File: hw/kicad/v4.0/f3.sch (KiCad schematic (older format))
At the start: 34 parts, among them P11 USB_OTG, P12 CONN_01X04, P7 CONN_01X04, T1 testpoint, T2 testpoint, T44 testpoint, T45 testpoint, T46 testpoint, U21 USBLC6-4SC6, U25 STM32F303CBTx, U29 USBLC6-4SC6, Y1 8M

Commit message: update TVS LCSC part number
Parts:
- U21, U29: LCSC C252436 -> C435848
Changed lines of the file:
@@
 EESchema Schematic File Version 4
-LIBS:stmbl_4.0-cache
 EELAYER 30 0
 EELAYER END
@@
 F 9 "" H 0   0   50  0001 C CNN "InternalName"
 F 10 "STMicroelectronics" H 0   0   50  0001 C CNN "Manufacturer"
-F 11 "C252436" H 9400 6600 50  0001 C CNN "LCSC"
+F 11 "C435848" H 9400 6600 50  0001 C CNN "LCSC"
 	1    9400 6600
 	1    0    0    -1
@@
 F 9 "" H 0   0   50  0001 C CNN "InternalName"
 F 10 "STMicroelectronics" H 0   0   50  0001 C CNN "Manufacturer"
-F 11 "C252436" H 4350 5650 50  0001 C CNN "LCSC"
+F 11 "C435848" H 4350 5650 50  0001 C CNN "LCSC"
 	1    4350 5650
 	1    0    0    -1

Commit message: Changed 120uf 1808 to 1210 100uF
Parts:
- C10, C128, C2, C7, C78, C79, C82, C83, C9: LCSC C14663 -> C14663
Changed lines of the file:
@@
 F 9 "" H 0   0   50  0001 C CNN "Description"
 F 10 "" H 0   0   50  0001 C CNN "Manufacturer"
-F 11 " C14663" H 9700 950 50  0001 C CNN "LCSC"
+F 11 "C14663" H 9700 950 50  0001 C CNN "LCSC"
 	1    9700 950
 	1    0    0    -1
@@
 F 9 "" H 0   0   50  0001 C CNN "Description"
 F 10 "" H 0   0   50  0001 C CNN "Manufacturer"
-F 11 " C14663" H 9800 950 50  0001 C CNN "LCSC"
+F 11 "C14663" H 9800 950 50  0001 C CNN "LCSC"
 	1    9800 950
 	1    0    0    -1
@@
 F 9 "" H 0   0   50  0001 C CNN "Description"
 F 10 "" H 0   0   50  0001 C CNN "Manufacturer"
-F 11 " C14663" H 9900 950 50  0001 C CNN "LCSC"
+F 11 "C14663" H 9900 950 50  0001 C CNN "LCSC"
 	1    9900 950
 	1    0    0    -1
@@
 F 9 "" H 0   0   50  0001 C CNN "Description"
 F 10 "" H 0   0   50  0001 C CNN "Manufacturer"
-F 11 " C14663" H 10000 950 50  0001 C CNN "LCSC"
+F 11 "C14663" H 10000 950 50  0001 C CNN "LCSC"
 	1    10000 950
 	1    0    0    -1
@@
 F 9 "" H 0   0   50  0001 C CNN "Description"
 F 10 "" H 0   0   50  0001 C CNN "Manufacturer"
-F 11 " C14663" H 7800 2150 50  0001 C CNN "LCSC"
+F 11 "C14663" H 7800 2150 50  0001 C CNN "LCSC"
 	1    7800 2150
 	1    0    0    -1
@@
 F 9 "" H 0   0   50  0001 C CNN "Description"
 F 10 "" H 0   0   50  0001 C CNN "Manufacturer"
-F 11 " C14663" H 8850 1500 50  0001 C CNN "LCSC"
+F 11 "C14663" H 8850 1500 50  0001 C CNN "LCSC"
 	1    8850 1500
 	0    1    1    0
@@
 F 9 "" H 0   0   50  0001 C CNN "Description"
 F 10 "" H 0   0   50  0001 C CNN "Manufacturer"
-F 11 " C14663" H 11000 1000 50  0001 C CNN "LCSC"
+F 11 "C14663" H 11000 1000 50  0001 C CNN "LCSC"
 	1    11000 1000
 	1    0    0    -1
@@
 F 9 "" H 0   0   50  0001 C CNN "Description"
 F 10 "" H 0   0   50  0001 C CNN "Manufacturer"
-F 11 " C14663" H 7450 6600 50  0001 C CNN "LCSC"
+F 11 "C14663" H 7450 6600 50  0001 C CNN "LCSC"
 	1    7450 6600
 	1    0    0    -1
@@
 F 9 "" H 0   0   50  0001 C CNN "Description"
 F 10 "" H 0   0   50  0001 C CNN "Manufacturer"
-F 11 " C14663" H 4100 6500 50  0001 C CNN "LCSC"
+F 11 "C14663" H 4100 6500 50  0001 C CNN "LCSC"
 	1    4100 6500
 	1    0    0    -1

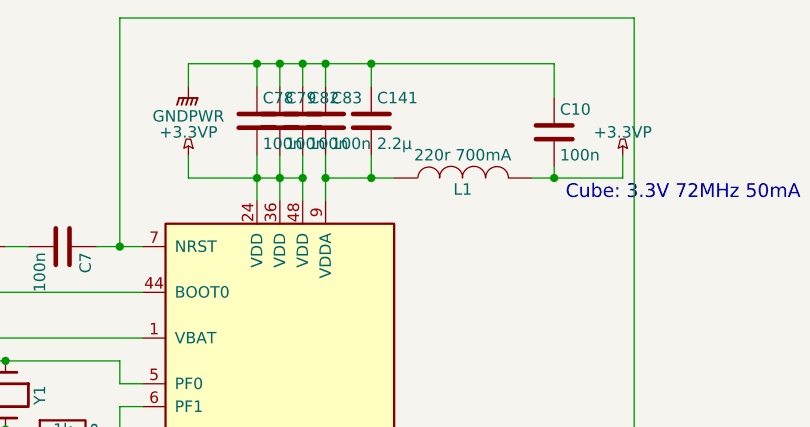
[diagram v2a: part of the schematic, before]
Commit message: Switch some 2.2uf 0603 to 1uf bypass to get 50V version on jlcpcb
Change 2.2uf 0603 to 0805 on iram to get 50V version on jlcpcb
other cleanup
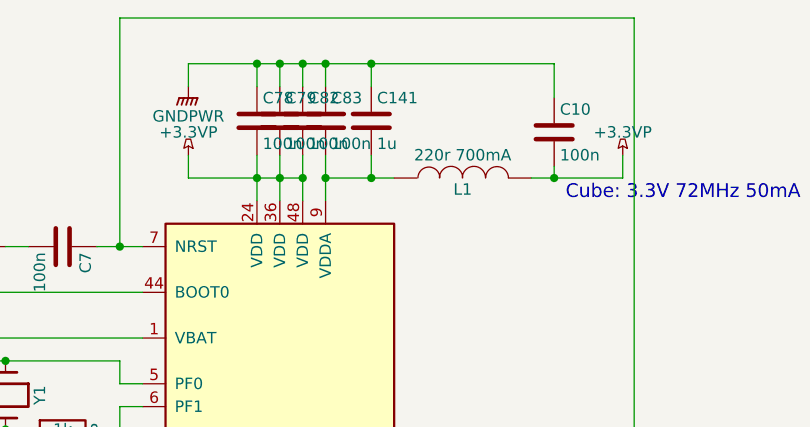
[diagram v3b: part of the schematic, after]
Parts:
- C10, C128, C2, C7, C78, C79, C82, C83, C9: Manufacturer (none) -> YAGEO; Manufacturer No (none) -> CC0603KRX7R9BB104
- C141: value 2.2µ -> 1u; LCSC C23630 -> C15849; Manufacturer (none) -> Samsung Electro-Mechanics; Manufacturer No (none) -> CL10A105KB8NNNC
- C5, C6: Manufacturer (none) -> Samsung Electro-Mechanics; Manufacturer No (none) -> CL10C180JB8NNNC
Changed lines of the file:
@@
 F 3 "" H 9700 950 60  0000 C CNN
 F 4 "" H 9700 950 60  0001 C CNN "InternalName"
-F 5 "" H 9700 950 60  0001 C CNN "Manufacturer No"
+F 5 "CC0603KRX7R9BB104 " H 9700 950 60  0001 C CNN "Manufacturer No"
 F 6 "50V" H 9700 950 60  0001 C CNN "Voltage"
 F 7 "" H 9700 950 60  0001 C CNN "Source"
 F 8 "X5R" H 9700 950 60  0001 C CNN "Tolerance"
 F 9 "" H 0   0   50  0001 C CNN "Description"
-F 10 "" H 0   0   50  0001 C CNN "Manufacturer"
+F 10 "YAGEO" H 0   0   50  0001 C CNN "Manufacturer"
 F 11 "C14663" H 9700 950 50  0001 C CNN "LCSC"
 	1    9700 950
@@
 F 3 "" H 9800 950 60  0000 C CNN
 F 4 "" H 9800 950 60  0001 C CNN "InternalName"
-F 5 "" H 9800 950 60  0001 C CNN "Manufacturer No"
+F 5 "CC0603KRX7R9BB104 " H 9800 950 60  0001 C CNN "Manufacturer No"
 F 6 "50V" H 9800 950 60  0001 C CNN "Voltage"
 F 7 "" H 9800 950 60  0001 C CNN "Source"
 F 8 "X5R" H 9800 950 60  0001 C CNN "Tolerance"
 F 9 "" H 0   0   50  0001 C CNN "Description"
-F 10 "" H 0   0   50  0001 C CNN "Manufacturer"
+F 10 "YAGEO" H 0   0   50  0001 C CNN "Manufacturer"
 F 11 "C14663" H 9800 950 50  0001 C CNN "LCSC"
 	1    9800 950
@@
 F 3 "" H 9900 950 60  0000 C CNN
 F 4 "" H 9900 950 60  0001 C CNN "InternalName"
-F 5 "" H 9900 950 60  0001 C CNN "Manufacturer No"
+F 5 "CC0603KRX7R9BB104 " H 9900 950 60  0001 C CNN "Manufacturer No"
 F 6 "50V" H 9900 950 60  0001 C CNN "Voltage"
 F 7 "" H 9900 950 60  0001 C CNN "Source"
 F 8 "X5R" H 9900 950 60  0001 C CNN "Tolerance"
 F 9 "" H 0   0   50  0001 C CNN "Description"
-F 10 "" H 0   0   50  0001 C CNN "Manufacturer"
+F 10 "YAGEO" H 0   0   50  0001 C CNN "Manufacturer"
 F 11 "C14663" H 9900 950 50  0001 C CNN "LCSC"
 	1    9900 950
@@
 F 3 "" H 10000 950 60  0000 C CNN
 F 4 "" H 10000 950 60  0001 C CNN "InternalName"
-F 5 "" H 10000 950 60  0001 C CNN "Manufacturer No"
+F 5 "CC0603KRX7R9BB104 " H 10000 950 60  0001 C CNN "Manufacturer No"
 F 6 "50V" H 10000 950 60  0001 C CNN "Voltage"
 F 7 "" H 10000 950 60  0001 C CNN "Source"
 F 8 "X5R" H 10000 950 60  0001 C CNN "Tolerance"
 F 9 "" H 0   0   50  0001 C CNN "Description"
-F 10 "" H 0   0   50  0001 C CNN "Manufacturer"
+F 10 "YAGEO" H 0   0   50  0001 C CNN "Manufacturer"
 F 11 "C14663" H 10000 950 50  0001 C CNN "LCSC"
 	1    10000 950
@@
 F 3 "" H 8350 2000 60  0000 C CNN
 F 4 "" H 8350 2000 60  0001 C CNN "InternalName"
-F 5 "" H 8350 2000 60  0001 C CNN "Manufacturer No"
+F 5 "CL10C180JB8NNNC" H 8350 2000 60  0001 C CNN "Manufacturer No"
 F 6 "50V" H 8350 2000 60  0001 C CNN "Voltage"
 F 7 "" H 8350 2000 60  0001 C CNN "Source"
 F 8 "X5R" H 8350 2000 60  0001 C CNN "Tolerance"
 F 9 "" H 0   0   50  0001 C CNN "Description"
-F 10 "" H 0   0   50  0001 C CNN "Manufacturer"
+F 10 "Samsung Electro-Mechanics" H 0   0   50  0001 C CNN "Manufacturer"
 F 11 "C1647" H 8350 2000 50  0001 C CNN "LCSC"
 	1    8350 2000
@@
 F 3 "" H 8350 2300 60  0000 C CNN
 F 4 "" H 8350 2300 60  0001 C CNN "InternalName"
-F 5 "" H 8350 2300 60  0001 C CNN "Manufacturer No"
+F 5 "CL10C180JB8NNNC" H 8350 2300 60  0001 C CNN "Manufacturer No"
 F 6 "50V" H 8350 2300 60  0001 C CNN "Voltage"
 F 7 "" H 8350 2300 60  0001 C CNN "Source"
 F 8 "X5R" H 8350 2300 60  0001 C CNN "Tolerance"
 F 9 "" H 0   0   50  0001 C CNN "Description"
-F 10 "" H 0   0   50  0001 C CNN "Manufacturer"
+F 10 "Samsung Electro-Mechanics" H 0   0   50  0001 C CNN "Manufacturer"
 F 11 "C1647" H 8350 2300 50  0001 C CNN "LCSC"
 	1    8350 2300
@@
 F 3 "" H 7800 2150 60  0000 C CNN
 F 4 "" H 7800 2150 60  0001 C CNN "InternalName"
-F 5 "" H 7800 2150 60  0001 C CNN "Manufacturer No"
+F 5 "CC0603KRX7R9BB104 " H 7800 2150 60  0001 C CNN "Manufacturer No"
 F 6 "50V" H 7800 2150 60  0001 C CNN "Voltage"
 F 7 "" H 7800 2150 60  0001 C CNN "Source"
 F 8 "X5R" H 7800 2150 60  0001 C CNN "Tolerance"
 F 9 "" H 0   0   50  0001 C CNN "Description"
-F 10 "" H 0   0   50  0001 C CNN "Manufacturer"
+F 10 "YAGEO" H 0   0   50  0001 C CNN "Manufacturer"
 F 11 "C14663" H 7800 2150 50  0001 C CNN "LCSC"
 	1    7800 2150
@@
 F 3 "" H 8850 1500 60  0000 C CNN
 F 4 "" H 8850 1500 60  0001 C CNN "InternalName"
-F 5 "" H 8850 1500 60  0001 C CNN "Manufacturer No"
+F 5 "CC0603KRX7R9BB104 " H 8850 1500 60  0001 C CNN "Manufacturer No"
 F 6 "50V" H 8850 1500 60  0001 C CNN "Voltage"
 F 7 "" H 8850 1500 60  0001 C CNN "Source"
 F 8 "X5R" H 8850 1500 60  0001 C CNN "Tolerance"
 F 9 "" H 0   0   50  0001 C CNN "Description"
-F 10 "" H 0   0   50  0001 C CNN "Manufacturer"
+F 10 "YAGEO" H 0   0   50  0001 C CNN "Manufacturer"
 F 11 "C14663" H 8850 1500 50  0001 C CNN "LCSC"
 	1    8850 1500
@@
 F 9 "" H 0   0   50  0001 C CNN "Description"
 F 10 "" H 0   0   50  0001 C CNN "Manufacturer"
+F 11 "" H 11650 4150 50  0001 C CNN "LCSC"
 	1    11650 4150
 	1    0    0    1
@@
 F 3 "" H 11000 1000 60  0000 C CNN
 F 4 "" H 11000 1000 60  0001 C CNN "InternalName"
-F 5 "" H 11000 1000 60  0001 C CNN "Manufacturer No"
+F 5 "CC0603KRX7R9BB104 " H 11000 1000 60  0001 C CNN "Manufacturer No"
 F 6 "50V" H 11000 1000 60  0001 C CNN "Voltage"
 F 7 "" H 11000 1000 60  0001 C CNN "Source"
 F 8 "X5R" H 11000 1000 60  0001 C CNN "Tolerance"
 F 9 "" H 0   0   50  0001 C CNN "Description"
-F 10 "" H 0   0   50  0001 C CNN "Manufacturer"
+F 10 "YAGEO" H 0   0   50  0001 C CNN "Manufacturer"
 F 11 "C14663" H 11000 1000 50  0001 C CNN "LCSC"
 	1    11000 1000
@@
 F 3 "" H 7450 6600 60  0000 C CNN
 F 4 "" H 7450 6600 60  0001 C CNN "InternalName"
-F 5 "" H 7450 6600 60  0001 C CNN "Manufacturer No"
+F 5 "CC0603KRX7R9BB104 " H 7450 6600 60  0001 C CNN "Manufacturer No"
 F 6 "50V" H 7450 6600 60  0001 C CNN "Voltage"
 F 7 "" H 7450 6600 60  0001 C CNN "Source"
 F 8 "X5R" H 7450 6600 60  0001 C CNN "Tolerance"
 F 9 "" H 0   0   50  0001 C CNN "Description"
-F 10 "" H 0   0   50  0001 C CNN "Manufacturer"
+F 10 "YAGEO" H 0   0   50  0001 C CNN "Manufacturer"
 F 11 "C14663" H 7450 6600 50  0001 C CNN "LCSC"
 	1    7450 6600
@@
 F 3 "" H 4100 6500 60  0000 C CNN
 F 4 "" H 4100 6500 60  0001 C CNN "InternalName"
-F 5 "" H 4100 6500 60  0001 C CNN "Manufacturer No"
+F 5 "CC0603KRX7R9BB104 " H 4100 6500 60  0001 C CNN "Manufacturer No"
 F 6 "50V" H 4100 6500 60  0001 C CNN "Voltage"
 F 7 "" H 4100 6500 60  0001 C CNN "Source"
 F 8 "X5R" H 4100 6500 60  0001 C CNN "Tolerance"
 F 9 "" H 0   0   50  0001 C CNN "Description"
-F 10 "" H 0   0   50  0001 C CNN "Manufacturer"
+F 10 "YAGEO" H 0   0   50  0001 C CNN "Manufacturer"
 F 11 "C14663" H 4100 6500 50  0001 C CNN "LCSC"
 	1    4100 6500
@@
 F 9 "" H 0   0   50  0001 C CNN "Description"
 F 10 "" H 0   0   50  0001 C CNN "Manufacturer"
+F 11 "" H 6100 6650 50  0001 C CNN "LCSC"
 	1    6100 6650
 	1    0    0    1
@@
 P 10200 950
 F 0 "C141" H 10225 1050 50  0000 L CNN
-F 1 "2.2µ" H 10225 850 50  0000 L CNN
+F 1 "1u" H 10225 850 50  0000 L CNN
 F 2 "stmbl:C_0603" H 10238 800 30  0001 C CNN
 F 3 "" H 10200 950 60  0000 C CNN
 F 4 "" H 10200 950 60  0001 C CNN "InternalName"
-F 5 "" H 10200 950 60  0001 C CNN "Manufacturer No"
+F 5 "CL10A105KB8NNNC" H 10200 950 60  0001 C CNN "Manufacturer No"
 F 6 "35V" H 10200 950 60  0001 C CNN "Voltage"
 F 7 "" H 10200 950 60  0001 C CNN "Source"
 F 8 "X5R" H 10200 950 60  0001 C CNN "Tolerance"
 F 9 "" H 0   0   50  0001 C CNN "Description"
-F 10 "" H 0   0   50  0001 C CNN "Manufacturer"
-F 11 "C23630" H 10200 950 50  0001 C CNN "LCSC"
+F 10 "Samsung Electro-Mechanics" H 0   0   50  0001 C CNN "Manufacturer"
+F 11 "C15849" H 10200 950 50  0001 C CNN "LCSC"
 	1    10200 950
 	1    0    0    -1

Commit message: Change Crystals to right footprint
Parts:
- Y1: LCSC C389778 -> C157341
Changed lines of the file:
@@
 F 9 "" H 0   0   50  0001 C CNN "Description"
 F 10 "Abracon LLC" H 0   0   50  0001 C CNN "Manufacturer"
-F 11 "C389778" H 8600 2150 50  0001 C CNN "LCSC"
+F 11 "C157341" H 8600 2150 50  0001 C CNN "LCSC"
 	1    8600 2150
 	0    1    1    0
